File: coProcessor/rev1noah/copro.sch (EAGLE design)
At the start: 97 parts, among them IC1 STM32F405RGT6, J1 USB_MINI-B_SMT, J2 79107-08, J3 693061010911, J4 30320-6002HB, T1 2N2222, T10 2N2222, T2 2N2222, T3 2N2222, T4 2N2222, T5 2N2222, T6 2N2222, T7 2N2222, T8 2N2222, T9 2N2222, U1 LM2597N-5.0, U2 SN65HVD232QD

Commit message: Slight progress on last commit, just so everything is up to date
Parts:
- added C5: 100pF, SparkFun-Capacitors:0.1UF-0603-100V-10%
- added CANH_R, CANL_R: LTST-S270GKT, LTST-S270GKT:LTST-S270GKT
- added R45: 60, SparkFun-Resistors:1KOHM-0603-1/10W-1%
- added R46, R47: 330, SparkFun-Resistors:1KOHM-0603-1/10W-1%
- renumbered U2 to CAN_TRANSCEIVER
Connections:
- net N$5 renamed RXD
- removed net N$12: CAN_TRANSCEIVER.CANL, U$1.CAN_L
- new net CANH: C5.2, CAN_TRANSCEIVER.CANH, R45.1, R46.2, U$1.CAN_H
- new net CANL: C5.1, CAN_TRANSCEIVER.CANL, R45.2, R47.2, U$1.CAN_L
- new net N$34: CANH_R.A2, R46.1
- net GND: now also CANH_R.K2, CANL_R.K2
- net N$8: now also CANL_R.A2, R47.1; no longer CAN_TRANSCEIVER.CANH, U$1.CAN_H
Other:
- note added: "SERIOUSLY DO NOT KNOW HOW TO HOOK THIS UP"
- note removed: "NEEDS WORK"
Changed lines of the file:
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@@
 <part name="GND29" library="supply1" library_urn="urn:adsk.eagle:library:371" deviceset="GND" device=""/>
 <part name="+3V3" library="supply1" library_urn="urn:adsk.eagle:library:371" deviceset="+3V3" device=""/>
-<part name="U2" library="SN65HVD232QD" deviceset="SN65HVD232QD" device=""/>
+<part name="CAN_TRANSCEIVER" library="SN65HVD232QD" deviceset="SN65HVD232QD" device=""/>
 <part name="J2" library="con-molex-milli-grid" deviceset="79107-08" device=""/>
 <part name="+3V9" library="supply1" library_urn="urn:adsk.eagle:library:371" deviceset="+3V3" device=""/>
+<part name="R45" library="SparkFun-Resistors" deviceset="1KOHM" device="-0603-1/10W-1%" value="60"/>
+<part name="C5" library="SparkFun-Capacitors" deviceset="0.1UF" device="-0603-100V-10%" value="100pF"/>
+<part name="GND30" library="supply1" library_urn="urn:adsk.eagle:library:371" deviceset="GND" device=""/>
+<part name="R46" library="SparkFun-Resistors" deviceset="1KOHM" device="-0603-1/10W-1%" value="330"/>
+<part name="R47" library="SparkFun-Resistors" deviceset="1KOHM" device="-0603-1/10W-1%" value="330"/>
+<part name="CANL_R" library="LTST-S270GKT" deviceset="LTST-S270GKT" device=""/>
+<part name="CANH_R" library="LTST-S270GKT" deviceset="LTST-S270GKT" device=""/>
+<part name="GND31" library="supply1" library_urn="urn:adsk.eagle:library:371" deviceset="GND" device=""/>
+<part name="GND32" library="supply1" library_urn="urn:adsk.eagle:library:371" deviceset="GND" device=""/>
 </parts>
 <sheets>
@@
 <text x="426.72" y="38.1" size="1.778" layer="91">5 v</text>
 <text x="408.94" y="71.12" size="1.778" layer="91">18 - 22 V</text>
-<text x="279.4" y="226.06" size="1.778" layer="91">NEEDS WORK</text>
-<text x="274.32" y="236.22" size="1.778" layer="91">NEEDS WORK</text>
-<text x="276.86" y="220.98" size="1.778" layer="91">NEEDS WORK</text>
-<text x="287.02" y="208.28" size="1.778" layer="91">NEEDS WORK</text>
-<text x="276.86" y="231.14" size="1.778" layer="91">NEEDS WORK</text>
-<text x="281.94" y="241.3" size="1.778" layer="91">NEEDS WORK</text>
-<text x="292.1" y="228.6" size="1.778" layer="91">NEEDS WORK</text>
-<text x="287.02" y="220.98" size="1.778" layer="91">NEEDS WORK</text>
-<text x="281.94" y="218.44" size="1.778" layer="91">NEEDS WORK</text>
+<text x="231.14" y="248.92" size="1.778" layer="91" rot="R90">SERIOUSLY DO NOT KNOW HOW TO HOOK THIS UP</text>
 </plain>
 <instances>
@@
 <instance part="GND29" gate="1" x="180.34" y="215.9"/>
 <instance part="+3V3" gate="G$1" x="180.34" y="269.24"/>
-<instance part="U2" gate="A" x="198.12" y="238.76"/>
+<instance part="CAN_TRANSCEIVER" gate="A" x="198.12" y="238.76"/>
 <instance part="J2" gate="G$1" x="91.44" y="66.04" rot="R90"/>
 <instance part="+3V9" gate="G$1" x="76.2" y="63.5"/>
+<instance part="R45" gate="G$1" x="228.6" y="241.3" rot="R90"/>
+<instance part="C5" gate="G$1" x="236.22" y="241.3"/>
+<instance part="GND30" gate="1" x="243.84" y="251.46"/>
+<instance part="R46" gate="G$1" x="297.18" y="215.9" rot="R180"/>
+<instance part="R47" gate="G$1" x="297.18" y="187.96" rot="R180"/>
+<instance part="CANL_R" gate="G$1" x="307.34" y="187.96" rot="R90"/>
+<instance part="CANH_R" gate="G$1" x="307.34" y="215.9" rot="R90"/>
+<instance part="GND31" gate="1" x="314.96" y="213.36"/>
+<instance part="GND32" gate="1" x="314.96" y="185.42"/>
 </instances>
 <busses>
@@
 <segment>
 <pinref part="GND29" gate="1" pin="GND"/>
-<pinref part="U2" gate="A" pin="GND"/>
+<pinref part="CAN_TRANSCEIVER" gate="A" pin="GND"/>
 <wire x1="180.34" y1="226.06" x2="180.34" y2="218.44" width="0.1524" layer="91"/>
+</segment>
+<segment>
+<pinref part="CANL_R" gate="G$1" pin="K2"/>
+<pinref part="GND32" gate="1" pin="GND"/>
+<wire x1="309.88" y1="187.96" x2="314.96" y2="187.96" width="0.1524" layer="91"/>
+</segment>
+<segment>
+<pinref part="CANH_R" gate="G$1" pin="K2"/>
+<pinref part="GND31" gate="1" pin="GND"/>
+<wire x1="309.88" y1="215.9" x2="314.96" y2="215.9" width="0.1524" layer="91"/>
 </segment>
 </net>
@@
 <wire x1="180.34" y1="243.84" x2="180.34" y2="266.7" width="0.1524" layer="91"/>
 <pinref part="+3V3" gate="G$1" pin="+3V3"/>
-<pinref part="U2" gate="A" pin="VCC"/>
+<pinref part="CAN_TRANSCEIVER" gate="A" pin="VCC"/>
 </segment>
 <segment>
@@
 <wire x1="160.02" y1="170.18" x2="160.02" y2="238.76" width="0.1524" layer="91"/>
 <wire x1="160.02" y1="238.76" x2="180.34" y2="238.76" width="0.1524" layer="91"/>
-<pinref part="U2" gate="A" pin="D"/>
-</segment>
-</net>
-<net name="N$5" class="0">
+<pinref part="CAN_TRANSCEIVER" gate="A" pin="D"/>
+</segment>
+</net>
+<net name="RXD" class="0">
 <segment>
 <pinref part="IC1" gate="G$1" pin="PA11"/>
@@
 <wire x1="172.72" y1="172.72" x2="220.98" y2="172.72" width="0.1524" layer="91"/>
 <wire x1="220.98" y1="172.72" x2="220.98" y2="236.22" width="0.1524" layer="91"/>
-<pinref part="U2" gate="A" pin="R"/>
+<pinref part="CAN_TRANSCEIVER" gate="A" pin="R"/>
 <wire x1="220.98" y1="236.22" x2="215.9" y2="236.22" width="0.1524" layer="91"/>
-</segment>
-</net>
-<net name="N$8" class="0">
-<segment>
-<pinref part="U$1" gate="G$1" pin="CAN_H"/>
-<pinref part="U2" gate="A" pin="CANH"/>
-<wire x1="287.02" y1="88.9" x2="287.02" y2="241.3" width="0.1524" layer="91"/>
-<wire x1="287.02" y1="241.3" x2="215.9" y2="241.3" width="0.1524" layer="91"/>
-</segment>
-</net>
-<net name="N$12" class="0">
-<segment>
-<pinref part="U$1" gate="G$1" pin="CAN_L"/>
-<pinref part="U2" gate="A" pin="CANL"/>
-<wire x1="281.94" y1="88.9" x2="281.94" y2="243.84" width="0.1524" layer="91"/>
-<wire x1="281.94" y1="243.84" x2="215.9" y2="243.84" width="0.1524" layer="91"/>
 </segment>
 </net>
@@
 </segment>
 </net>
+<net name="CANH" class="0">
+<segment>
+<pinref part="R45" gate="G$1" pin="1"/>
+<pinref part="C5" gate="G$1" pin="2"/>
+<wire x1="228.6" y1="236.22" x2="236.22" y2="236.22" width="0.1524" layer="91"/>
+<wire x1="236.22" y1="236.22" x2="236.22" y2="238.76" width="0.1524" layer="91"/>
+<wire x1="228.6" y1="236.22" x2="223.52" y2="236.22" width="0.1524" layer="91"/>
+<junction x="228.6" y="236.22"/>
+<wire x1="223.52" y1="236.22" x2="223.52" y2="241.3" width="0.1524" layer="91"/>
+<pinref part="CAN_TRANSCEIVER" gate="A" pin="CANH"/>
+<wire x1="223.52" y1="241.3" x2="215.9" y2="241.3" width="0.1524" layer="91"/>
+<wire x1="236.22" y1="236.22" x2="287.02" y2="236.22" width="0.1524" layer="91"/>
+<junction x="236.22" y="236.22"/>
+<pinref part="U$1" gate="G$1" pin="CAN_H"/>
+<wire x1="287.02" y1="236.22" x2="287.02" y2="215.9" width="0.1524" layer="91"/>
+<wire x1="287.02" y1="215.9" x2="287.02" y2="88.9" width="0.1524" layer="91"/>
+<wire x1="287.02" y1="86.36" x2="287.02" y2="88.9" width="0.1524" layer="91"/>
+<pinref part="R46" gate="G$1" pin="2"/>
+<wire x1="292.1" y1="215.9" x2="287.02" y2="215.9" width="0.1524" layer="91"/>
+<junction x="287.02" y="215.9"/>
+</segment>
+</net>
+<net name="N$8" class="0">
+<segment>
+<pinref part="R47" gate="G$1" pin="1"/>
+<pinref part="CANL_R" gate="G$1" pin="A2"/>
+</segment>
+</net>
+<net name="N$34" class="0">
+<segment>
+<pinref part="R46" gate="G$1" pin="1"/>
+<pinref part="CANH_R" gate="G$1" pin="A2"/>
+</segment>
+</net>
+<net name="CANL" class="0">
+<segment>
+<pinref part="R45" gate="G$1" pin="2"/>
+<pinref part="C5" gate="G$1" pin="1"/>
+<wire x1="228.6" y1="246.38" x2="236.22" y2="246.38" width="0.1524" layer="91"/>
+<pinref part="CAN_TRANSCEIVER" gate="A" pin="CANL"/>
+<wire x1="215.9" y1="243.84" x2="223.52" y2="243.84" width="0.1524" layer="91"/>
+<wire x1="223.52" y1="243.84" x2="223.52" y2="246.38" width="0.1524" layer="91"/>
+<wire x1="223.52" y1="246.38" x2="228.6" y2="246.38" width="0.1524" layer="91"/>
+<junction x="228.6" y="246.38"/>
+<pinref part="U$1" gate="G$1" pin="CAN_L"/>
+<wire x1="281.94" y1="88.9" x2="281.94" y2="187.96" width="0.1524" layer="91"/>
+<wire x1="281.94" y1="187.96" x2="281.94" y2="246.38" width="0.1524" layer="91"/>
+<wire x1="281.94" y1="246.38" x2="236.22" y2="246.38" width="0.1524" layer="91"/>
+<junction x="236.22" y="246.38"/>
+<pinref part="GND30" gate="1" pin="GND"/>
+<wire x1="236.22" y1="246.38" x2="236.22" y2="254" width="0.1524" layer="91"/>
+<wire x1="236.22" y1="254" x2="243.84" y2="254" width="0.1524" layer="91"/>
+<pinref part="R47" gate="G$1" pin="2"/>
+<wire x1="292.1" y1="187.96" x2="281.94" y2="187.96" width="0.1524" layer="91"/>
+<junction x="281.94" y="187.96"/>
+</segment>
+</net>

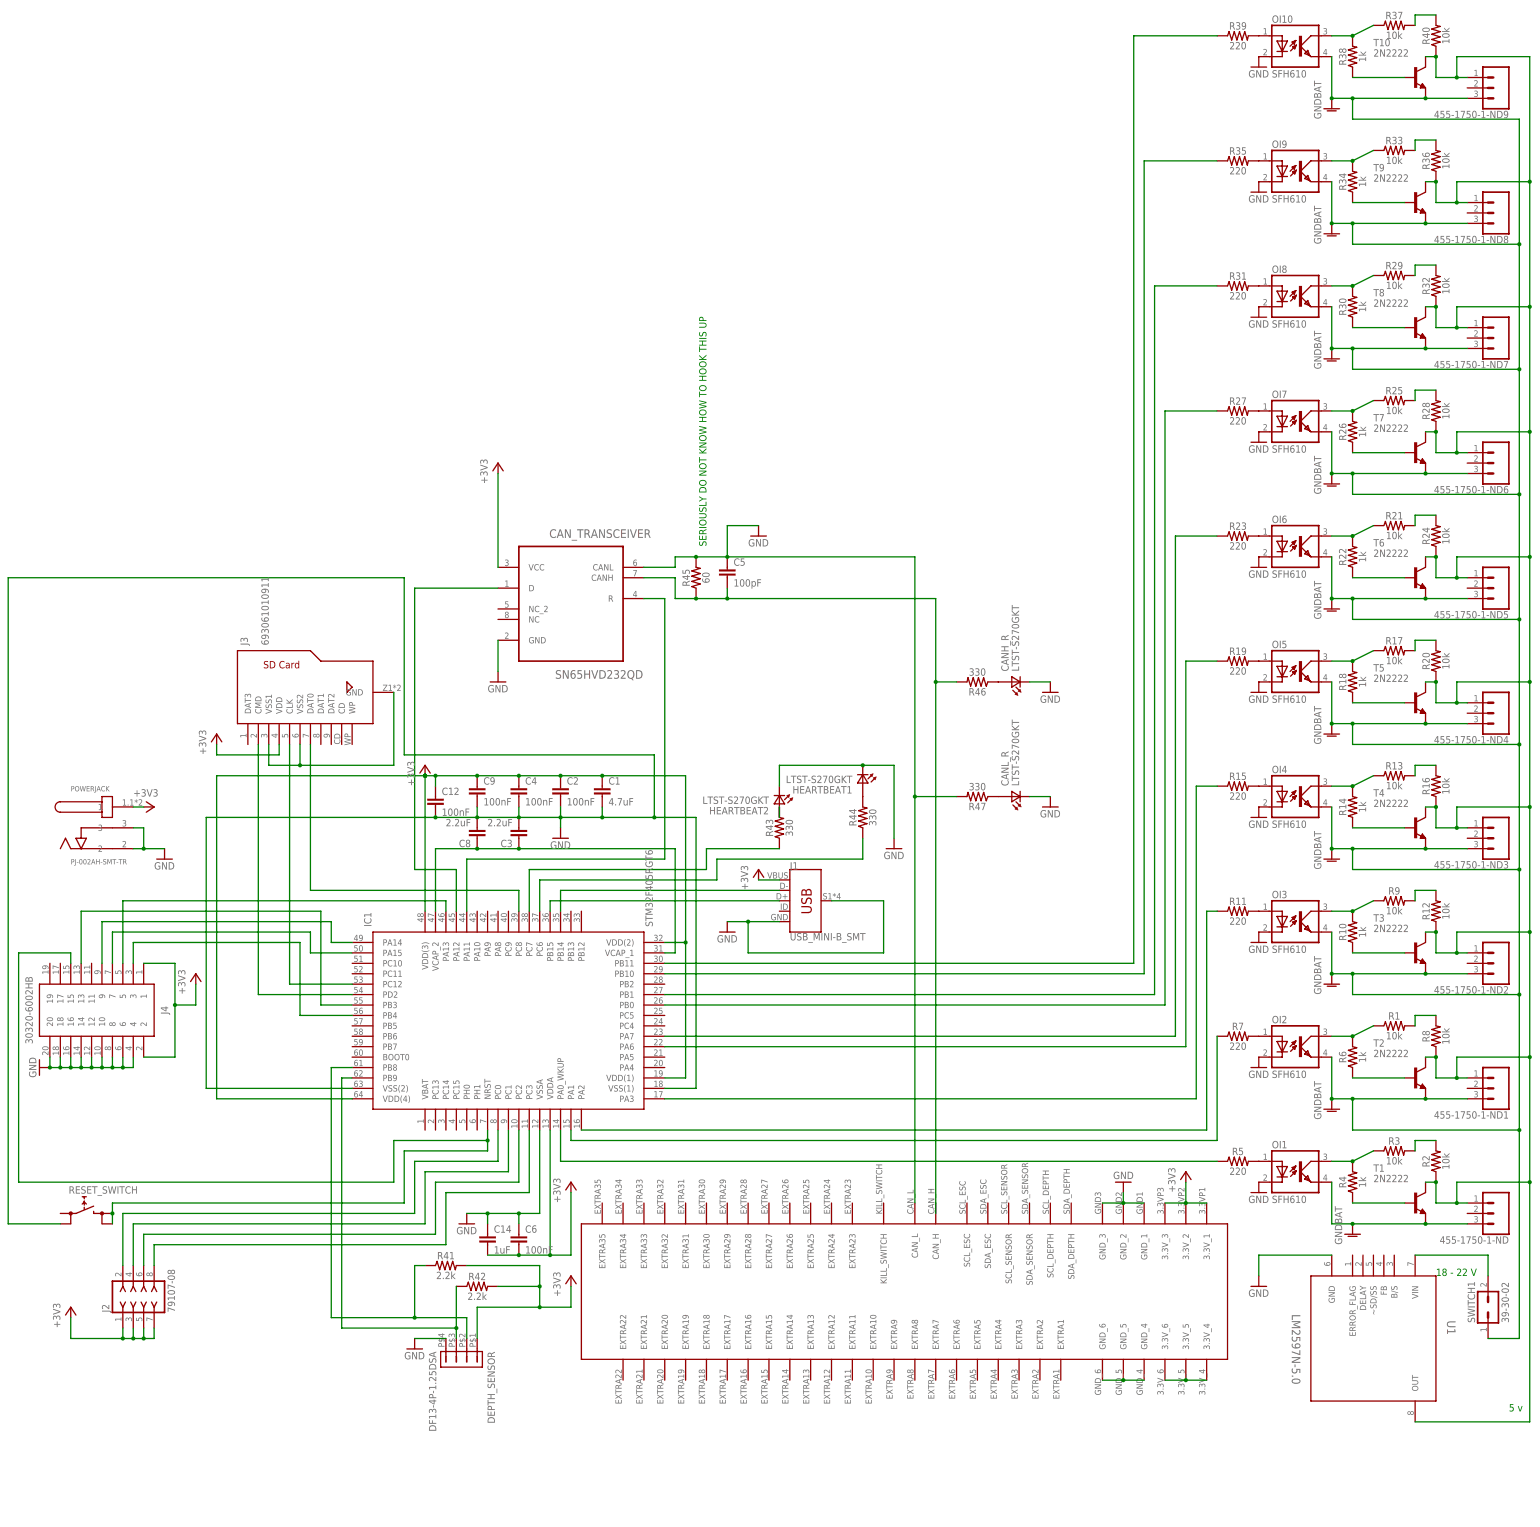
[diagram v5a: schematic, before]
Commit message: The current official coprocessor board is now saved under the filename "copro - copy". I will change that. More importantly, the board is tentatively finished, atleast enough for others to check it, which i highly suggest.
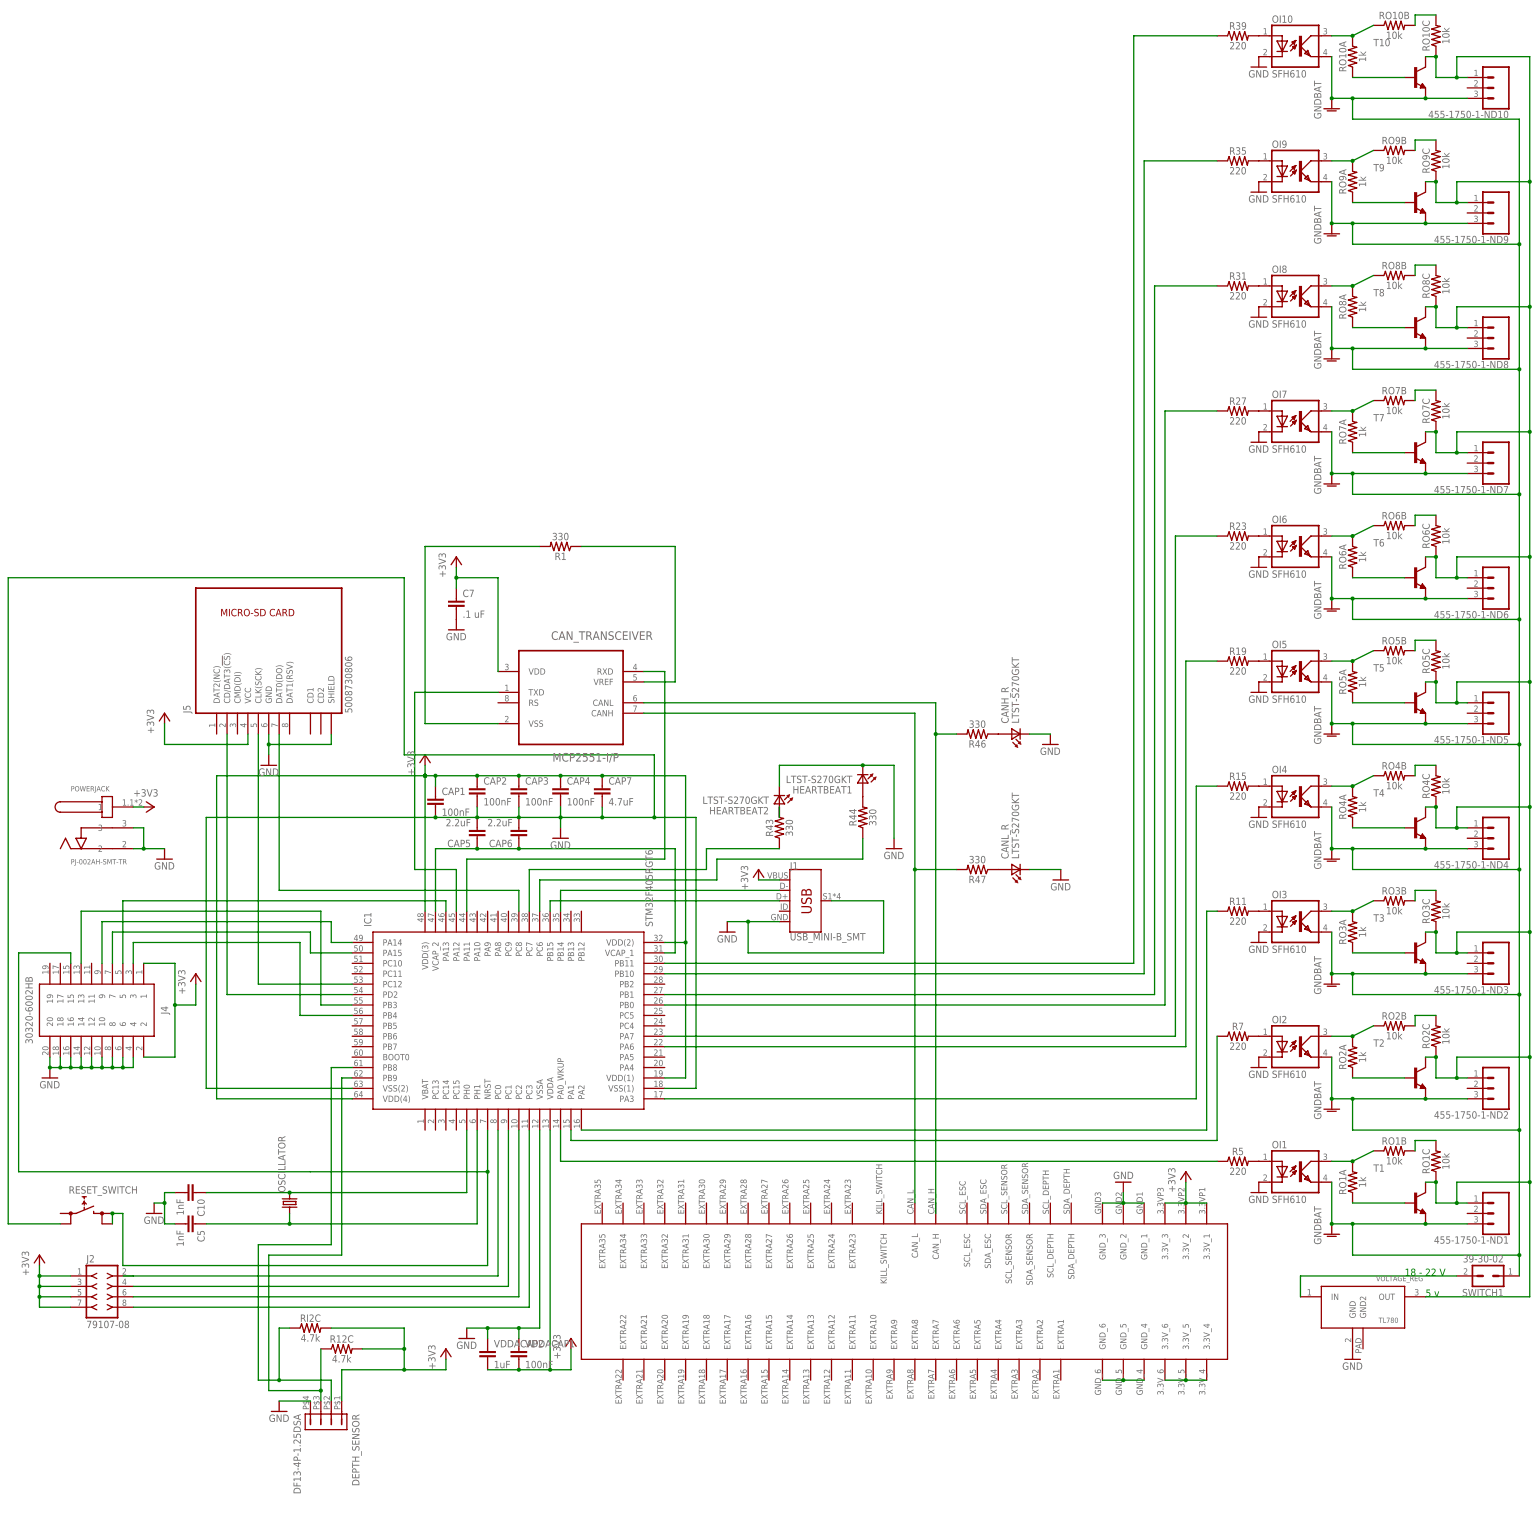
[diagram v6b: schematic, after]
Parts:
- removed 455-1750-1-ND: (no value), SparkFun-Connectors:CONN_03
- removed C14: 1uF, SparkFun-Capacitors:0.1UF-0603-100V-10%
- removed C6: 100nF, SparkFun-Capacitors:0.1UF-0603-100V-10%
- removed J3: 693061010911, 693061010911:693061010911
- removed R41, R42: 2.2k, SparkFun-Resistors:1KOHM-0603-1/10W-1%
- removed R45: 60, SparkFun-Resistors:1KOHM-0603-1/10W-1%
- removed U1: LM2597N-5.0, LM2597N-5.0:LM2597N-5.0
- added 455-1750-1-ND10: (no value), SparkFun-Connectors:CONN_03
- added C10: 1nF, SparkFun-Capacitors:0.1UF-0603-100V-10%
- added C7: .1 uF, SparkFun-Capacitors:0.1UF-0603-100V-10%
- added J5: 5008730806, 5008730806:5008730806
- added OSCILLATOR: (no value), crystal:CRYSTALHC49S
- added R12C, RI2C: 4.7k, SparkFun-Resistors:1KOHM-0603-1/10W-1%
- added RO2B: 10k, SparkFun-Resistors:1KOHM-0603-1/10W-1%
- added VDDACAP1: 100nF, SparkFun-Capacitors:0.1UF-0603-100V-10%
- added VDDACAP2: 1uF, SparkFun-Capacitors:0.1UF-0603-100V-10%
- added VOLTAGE_REG: TL780_VREG, TL780_VREG:TL780_VREG
- C5: value 100pF -> 1nF
- CAN_TRANSCEIVER: value SN65HVD232QD -> MCP2551-I/P; device SN65HVD232QD:SN65HVD232QD -> MCP2551-I_P:MCP2551-I/P
- R1: value 10k -> 330
- T1, T10, T2, T3, T4, T5, T6, T7, T8, T9: value 2N2222 -> (none); device transistor:2N2222 -> transistor:-NPN-TO126V
- renumbered C1 to CAP7, C12 to CAP1, C2 to CAP4, C3 to CAP6, C4 to CAP3, C8 to CAP5, C9 to CAP2, R10 to RO3A, R12 to RO3C, R13 to RO4B, R14 to RO4A, R16 to RO4C, R17 to RO5B, R18 to RO5A, R2 to RO1C, R20 to RO5C, R21 to RO6B, R22 to RO6A, R24 to RO6C, R25 to RO7B, R26 to RO7A, R28 to RO7C, R29 to RO8B, R3 to RO1B, R30 to RO8A, R32 to RO8C, R33 to RO9B, R34 to RO9A, R36 to RO9C, R37 to RO10B, R38 to RO10A, R4 to RO1A, R40 to RO10C, R6 to RO2A, R8 to RO2C, R9 to RO3B
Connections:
- net N$20 renamed 2
- net N$25 renamed 4
- net N$27 renamed 6
- net N$3 renamed VCAP_2TO1
- net N$32 renamed 8
- removed net +3V3: C14.2, C6.2, CAN_TRANSCEIVER.VCC, CAP1.1, CAP2.1, CAP3.1, CAP4.1, CAP7.1, DEPTH_SENSOR.1, IC1.VDD(1), IC1.VDD(2), IC1.VDD(3), IC1.VDD(4), IC1.VDDA, J1.VBUS, J2.1, J2.3, J2.5, J2.7, J3.VDD, J4.1, J4.2, POWERJACK.1, R41.2, R42.2
- removed net GNDA: 455-1750-1-ND1.3, 455-1750-1-ND2.3, 455-1750-1-ND3.3, 455-1750-1-ND4.3, 455-1750-1-ND5.3, 455-1750-1-ND6.3, 455-1750-1-ND7.3, 455-1750-1-ND8.3, 455-1750-1-ND9.3, OI10.EMIT, OI2.EMIT, OI3.EMIT, OI4.EMIT, OI5.EMIT, OI6.EMIT, OI7.EMIT, OI8.EMIT, OI9.EMIT, SWITCH1.1, T10.E, T2.E, T3.E, T4.E, T5.E, T6.E, T7.E, T8.E, T9.E
- removed net N$21: J3.GND, J3.VSS1, J3.VSS2
- removed net PB8: DEPTH_SENSOR.2, IC1.PB8, R41.1
- new net N$12: CAN_TRANSCEIVER.VREF, R1.1
- new net N$5: CAN_TRANSCEIVER.VSS, R1.2
- new net OSC1: C5.1, IC1.PH1, OSCILLATOR.1
- new net OSC2: C10.1, IC1.PH0, OSCILLATOR.2
- new net P$2: DEPTH_SENSOR.2, IC1.PB8, RI2C.1
- net 3.3V: now also C7.1, CAN_TRANSCEIVER.VDD, CAP1.1, CAP2.1, CAP3.1, CAP4.1, CAP7.1, DEPTH_SENSOR.1, IC1.VDD(1), IC1.VDD(2), IC1.VDD(3), IC1.VDD(4), IC1.VDDA, J1.VBUS, J2.1, J2.3, J2.5, J2.7, J4.1, J4.2, J5.VCC, POWERJACK.1, R12C.2, RI2C.2, VDDACAP1.2, VDDACAP2.2
- net CANH: now also CAN_TRANSCEIVER.CANL; no longer C5.2, CAN_TRANSCEIVER.CANH, R45.1
- net CANL: now also CAN_TRANSCEIVER.CANH; no longer C5.1, CAN_TRANSCEIVER.CANL, R45.2
- net CLK: now also J5.CLK(SCK); no longer J3.CLK
- net CMD: now also J5.CD/DAT3(!CS!); no longer J3.CMD
- net DATO: now also J5.DAT0(DO); no longer J3.DAT0
- net GND: now also C10.2, C5.2, C7.2, J5.GND, J5.SHIELD, VDDACAP1.1, VDDACAP2.1, VOLTAGE_REG.GND; no longer C14.1, C6.1, CAN_TRANSCEIVER.GND, U1.GND
- net GNDBAT: now also 455-1750-1-ND1.3, 455-1750-1-ND10.3, 455-1750-1-ND2.3, 455-1750-1-ND3.3, 455-1750-1-ND4.3, 455-1750-1-ND5.3, 455-1750-1-ND6.3, 455-1750-1-ND7.3, 455-1750-1-ND8.3, 455-1750-1-ND9.3, OI10.EMIT, OI2.EMIT, OI3.EMIT, OI4.EMIT, OI5.EMIT, OI6.EMIT, OI7.EMIT, OI8.EMIT, OI9.EMIT, SWITCH1.1, T10.E, T2.E, T3.E, T4.E, T5.E, T6.E, T7.E, T8.E, T9.E; no longer 455-1750-1-ND.3
- net N$1: now also RO2B.1; no longer R1.1
- net N$15: now also RO2B.2; no longer R1.2
- net N$18: now also 455-1750-1-ND10.1, VOLTAGE_REG.OUT; no longer 455-1750-1-ND.1, U1.OUT
- net N$7: now also VOLTAGE_REG.IN; no longer U1.VIN
- net PS$3: now also R12C.1; no longer R42.1
- net RXD: now also CAN_TRANSCEIVER.RXD; no longer CAN_TRANSCEIVER.R
- net TXD: now also CAN_TRANSCEIVER.TXD; no longer CAN_TRANSCEIVER.D
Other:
- note removed: "SERIOUSLY DO NOT KNOW HOW TO HOOK THIS UP"
- moved on the sheet: 455-1750-1-ND1, 455-1750-1-ND2, 455-1750-1-ND3, 455-1750-1-ND4, 455-1750-1-ND5, 455-1750-1-ND6, 455-1750-1-ND7, 455-1750-1-ND8, 455-1750-1-ND9, C5, CANH_R, CANL_R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
